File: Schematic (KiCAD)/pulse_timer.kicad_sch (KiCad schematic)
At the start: 50 parts, among them J66 Counter 4 Preload, J70 Counter 4 Preload

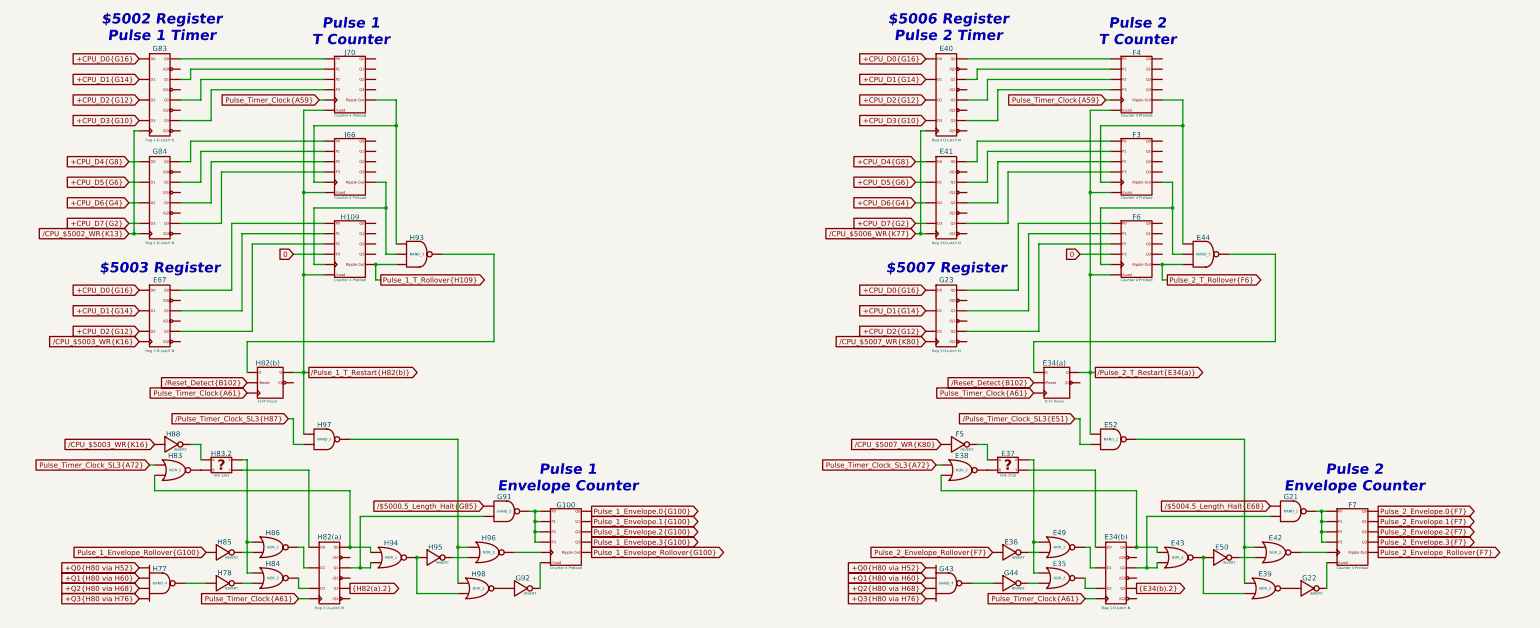
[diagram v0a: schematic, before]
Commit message: - Lots of additional comments and signal name improvements.  - "Don't know what this is yet but it is important" section of the pulse channels:    - I worked out the logic and it is a 4-bit binary up-counter with preload, made from gates and D-latches instead of T-flip-flops.    - It is extremely similar to the envelope counter, but takes twice the die space and much more traces.    - None of its outputs go anywhere else, so I believe that it has no actual function.    - It seems to be a previous attempt at making the envelope counter and it got disconnected and left in.    - Each pulse channel has its own copy and I moved both of them to the "Artifacts" sheet.    - The wasted space amounts to about half of one of the large columns on the left side of the die.  - A couple of "OAI2" cells that noted "unclear order": I determined the correct order of the inputs based on several others which were known.  - Deduced the purpose of the 2 separate methods of scanline detection:    - The one looking for 3 consecutive reads finds the start of a scanline.    - The one counting PPU /RD to find PPU cycle 336, finds the end of the scanline.    - I moved these beside each other on the same sheet for clarity.  - A66.5 Changed from Nand to Nor in order to make sense.  - Basic test mode:    - Pin 92: Active low, enables test mode.    - Pin 29: In test mode, it gives external control of "Scanline Start Detection", which is normally done with the familiar 3 matching PPU reads.  When not in test mode, the pin has no function.    - Pin 30: In test mode, it gives external control of "Scanline End Detection", which is normally done by counting PPU /RD to find PPU cycle 336.  It also gives control of "Pulse Length Clock" when in test mode.  When not in test mode, the pin has no function.    - Pin 98/SL3: In test mode, it gives external control of "Pulse Timer Clock".  Whether or not in test mode, this pin low makes the MMC5 pretend $5104 had not yet been written since reset, probably as a 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
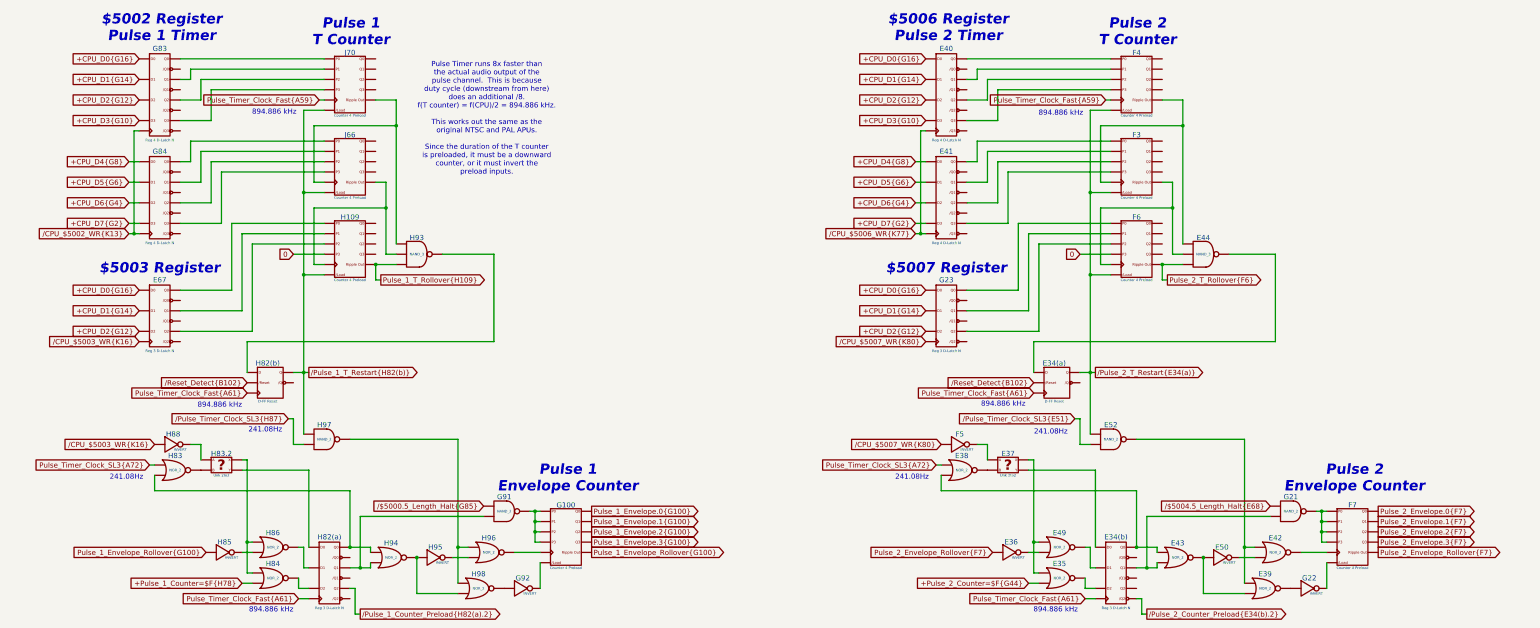
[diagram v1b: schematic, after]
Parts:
- removed G43, H77: NAND_4, symbol MMC5:NAND_4
- removed G44, H78: INVERT, symbol MMC5:INVERT
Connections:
- net {E34(b).2} is gone; now on net /Pulse_2_Counter_Preload{E34(b).2}: E34(b). (/Q2)
- net {H82(a).2} is gone; now on net /Pulse_1_Counter_Preload{H82(a).2}: H82(a). (/Q2)
- net at H86. (X): now also H83.2. (Y), H84. (X); no longer H85. (X)
- net at H83.2. (Y): now also H88. (X); no longer H83. (X)
- net /Pulse_2_Counter_Preload{E34(b).2}: now reaches E34(b). (/Q2)
- net at E37. (Y): now also E38. (X); no longer E34(b). (/Q2)
- net +Pulse_2_Counter=$F{G44}: now reaches E35. (X)
- net +Pulse_2_Counter=$F{G44}: no longer E34(b). (/Q2)
- net at E49. (X): now also E36. (X); no longer E34(b). (/Q2)
- net /Pulse_1_Counter_Preload{H82(a).2}: now reaches H82(a). (/Q2)
- net /Pulse_1_Counter_Preload{H82(a).2}: no longer H86. (X)
- net +Pulse_1_Counter=$F{H78}: now reaches H84. (X)
- net +Pulse_1_Counter=$F{H78}: no longer H82(a). (/Q2)
- net at H96. (X): now also H97. (X), H98. (X); no longer G100. (Ripple_Out)
- net at G92. (X): now also H98. (X); no longer G100. (Ripple_Out)
- net at E42. (X): now also E50. (X); no longer F7. (Ripple_Out)
- net at E50. (X): now also E39. (X), E43. (X); no longer E42. (X)
- removed net Pulse_Timer_Clock{A59}: F4. (Ripple_Out), J70. (Ripple_Out)
- removed net Pulse_Timer_Clock{A61}: E34(a). (/Q), E34(b). (/Q2), H82(a). (/Q2), H82(b). (/Q)
- new net: F6. (Ripple_Out), G23. (/Q2) (x3)
- new net: H85. (X), H86. (X)
- new net: H82(a). (/Q2), H83. (X), H94. (X)
- new net: H83. (X), H83.2. (Y)
- new net: E40. (/Q3), F4. (Ripple_Out) (x4)
- new net: E34(b). (/Q2), E37. (Y)
- new net: E34(b). (/Q2), E43. (X), G21. (X)
- new net: E34(b). (/Q2), E35. (X)
- new net: E34(b). (/Q2), E49. (X)
- new net: E34(b). (/Q2), E38. (X), E43. (X)
- new net: E35. (X), E37. (Y), E49. (X)
- new net: E37. (Y), F5. (X)
- new net: H109. (Ripple_Out), H93. (X), J66. (Ripple_Out)
- new net: H93. (X), J66. (Ripple_Out), J70. (Ripple_Out)
- new net: H82(b). (/Q), H93. (X)
- new net: E67. (/Q2), H109. (Ripple_Out) (x3)
- new net: F7. (Ripple_Out), G21. (X)
- new net: H82(a). (/Q2), H86. (X)
- new net: G91. (X), H82(a). (/Q2), H94. (X)
- new net: G100. (Ripple_Out), G91. (X)
- new net: E41. (/Q3), F3. (Ripple_Out) (x4)
- new net: E44. (X), F3. (Ripple_Out), F6. (Ripple_Out)
- new net: H82(a). (/Q2), H83.2. (Y)
- new net: H82(a). (/Q2), H84. (X)
- new net: H94. (X), H95. (X), H98. (X)
- new net: G100. (Ripple_Out), H96. (X)
- new net: G100. (Ripple_Out), G92. (X)
- new net: G84. (/Q3), J66. (Ripple_Out) (x4)
- new net: E39. (X), E42. (X), E52. (X)
- new net: E42. (X), F7. (Ripple_Out)
- new net: E44. (X), F3. (Ripple_Out), F4. (Ripple_Out)
- new net: G83. (/Q3), J70. (Ripple_Out) (x4)
- new net: E34(a). (/Q), E44. (X)
- new net Pulse_Timer_Clock_Fast{A59}: F4. (Ripple_Out), J70. (Ripple_Out)
- new net Pulse_Timer_Clock_Fast{A61}: E34(a). (/Q), E34(b). (/Q2), H82(a). (/Q2), H82(b). (/Q)
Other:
- note added: "241.08Hz"
- note added: "894.886 kHz"
- note added: "Pulse Timer runs 8x faster than the actual audio output of the pulse channel. This is because duty cycle (downstream from here) does an additional /8. f(T counter) = f(CPU)/2 = 894.886 kHz. This works out the same as the original NTSC and PAL APUs. Since the duration of the T counter is preloaded, it must be a downward counter, or it must invert the preload inputs."

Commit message: - Updated all of the various And-OR-Invert gates to have consistent names.  - Added the schematic for CL3 / SL3 GPIO pins.  There are no surprises revealed by this.  - Finished up the CPU address decoding tracing.  - Added one of the 'artifact' counters from the pulse channels
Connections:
- net at H86. (X): now also H83.2. (Y), H84. (X); no longer H85. (X)
- net at H83.2. (Y): now also H88. (X); no longer H83. (X)
- net at E37. (Y): now also E38. (X); no longer E34(b). (/Q2)
- net at E49. (X): now also E36. (X); no longer E34(b). (/Q2)
- net at H96. (X): now also H97. (X), H98. (X); no longer G100. (Ripple_Out)
- net at G92. (X): now also H98. (X); no longer G100. (Ripple_Out)
- net at E42. (X): now also E50. (X); no longer F7. (Ripple_Out)
- net at E50. (X): now also E39. (X), E43. (X); no longer E42. (X)
- new net: F6. (Ripple_Out), G23. (/Q2) (x3)
- new net: H85. (X), H86. (X)
- new net: H82(a). (/Q2), H83. (X), H94. (X)
- new net: H83. (X), H83.2. (Y)
- new net: E40. (/Q3), F4. (Ripple_Out) (x4)
- new net: E34(b). (/Q2), E37. (Y)
- new net: E34(b). (/Q2), E43. (X), G21. (X)
- new net: E34(b). (/Q2), E35. (X)
- new net: E34(b). (/Q2), E49. (X)
- new net: E34(b). (/Q2), E38. (X), E43. (X)
- new net: E35. (X), E37. (Y), E49. (X)
- new net: E37. (Y), F5. (X)
- new net: H109. (Ripple_Out), H93. (X), J66. (Ripple_Out)
- new net: H93. (X), J66. (Ripple_Out), J70. (Ripple_Out)
- new net: H82(b). (/Q), H93. (X)
- new net: E67. (/Q2), H109. (Ripple_Out) (x3)
- new net: F7. (Ripple_Out), G21. (X)
- new net: H82(a). (/Q2), H86. (X)
- new net: G91. (X), H82(a). (/Q2), H94. (X)
- new net: G100. (Ripple_Out), G91. (X)
- new net: E41. (/Q3), F3. (Ripple_Out) (x4)
- new net: E44. (X), F3. (Ripple_Out), F6. (Ripple_Out)
- new net: H82(a). (/Q2), H83.2. (Y)
- new net: H82(a). (/Q2), H84. (X)
- new net: H94. (X), H95. (X), H98. (X)
- new net: G100. (Ripple_Out), H96. (X)
- new net: G100. (Ripple_Out), G92. (X)
- new net: G84. (/Q3), J66. (Ripple_Out) (x4)
- new net: E39. (X), E42. (X), E52. (X)
- new net: E42. (X), F7. (Ripple_Out)
- new net: E44. (X), F3. (Ripple_Out), F4. (Ripple_Out)
- new net: G83. (/Q3), J70. (Ripple_Out) (x4)
- new net: E34(a). (/Q), E44. (X)
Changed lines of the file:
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@@
 	)
 	(symbol
+		(lib_name "Reg_3_D-Latch_N_1")
 		(lib_id "MMC5:Reg_3_D-Latch_N")
 		(at 243.84 81.28 0)
@@
 	)
 	(symbol
-		(lib_name "INVERT_2")
 		(lib_id "MMC5:INVERT")
 		(at 66.04 148.59 0)
@@
 	)
 	(symbol
-		(lib_name "NOR_2_2")
 		(lib_id "MMC5:NOR_2")
 		(at 53.34 128.27 0)
@@
 	)
 	(symbol
-		(lib_name "Reg_4_D-Latch_N_1")
+		(lib_name "Reg_4_D-Latch_N_2")
 		(lib_id "MMC5:Reg_4_D-Latch_N")
 		(at 243.84 24.13 0)
@@
 	)
 	(symbol
-		(lib_name "Reg_3_D-Latch_N_2")
 		(lib_id "MMC5:Reg_3_D-Latch_N")
 		(at 285.75 144.78 0)
@@
 	)
 	(symbol
-		(lib_name "UNKNOWN_2to2_1")
 		(lib_id "MMC5:UNKNOWN_2to2")
 		(at 259.08 129.54 0)
@@
 	)
 	(symbol
-		(lib_name "Counter_4_Preload_7")
 		(lib_id "MMC5:Counter_4_Preload")
 		(at 96.52 71.12 0)
@@
 	)
 	(symbol
-		(lib_name "NAND_2_2")
+		(lib_name "NAND_2_1")
 		(lib_id "MMC5:NAND_2")
 		(at 328.93 138.43 0)
@@
 	)
 	(symbol
-		(lib_name "Reg_3_D-Latch_N_1")
+		(lib_name "Reg_3_D-Latch_N_2")
 		(lib_id "MMC5:Reg_3_D-Latch_N")
 		(at 49.53 81.28 0)
@@
 	)
 	(symbol
+		(lib_name "NOR_2_1")
 		(lib_id "MMC5:NOR_2")
 		(at 77.47 147.32 0)
@@
 	)
 	(symbol
-		(lib_name "INVERT_7")
+		(lib_name "INVERT_3")
 		(lib_id "MMC5:INVERT")
 		(at 260.35 148.59 0)
@@
 	)
 	(symbol
-		(lib_name "Reg_4_D-Latch_N_2")
+		(lib_name "Reg_4_D-Latch_N_1")
 		(lib_id "MMC5:Reg_4_D-Latch_N")
 		(at 243.84 49.53 0)
@@
 	)
 	(symbol
-		(lib_name "Counter_4_Preload_2")
+		(lib_name "Counter_4_Preload_1")
 		(lib_id "MMC5:Counter_4_Preload")
 		(at 290.83 71.12 0)
@@
 	)
 	(symbol
-		(lib_name "INVERT_4")
+		(lib_name "INVERT_1")
 		(lib_id "MMC5:INVERT")
 		(at 118.11 149.86 0)
@@
 	)
 	(symbol
-		(lib_name "Counter_4_Preload_3")
+		(lib_name "Counter_4_Preload_2")
 		(lib_id "MMC5:Counter_4_Preload")
 		(at 149.86 142.24 0)
@@
 	)
 	(symbol
-		(lib_name "Reg_4_D-Latch_N_5")
 		(lib_id "MMC5:Reg_4_D-Latch_N")
 		(at 49.53 49.53 0)
@@
 	)
 	(symbol
-		(lib_name "NOR_2_6")
+		(lib_name "NOR_2_7")
 		(lib_id "MMC5:NOR_2")
 		(at 325.12 148.59 0)
@@
 	)
 	(symbol
-		(lib_name "NOR_2_9")
+		(lib_name "NOR_2_2")
 		(lib_id "MMC5:NOR_2")
 		(at 271.78 154.94 0)
@@
 	)
 	(symbol
+		(lib_name "Counter_4_Preload_3")
 		(lib_id "MMC5:Counter_4_Preload")
 		(at 290.83 30.48 0)
@@
 	)
 	(symbol
-		(lib_name "Counter_4_Preload_6")
+		(lib_name "Counter_4_Preload_4")
 		(lib_id "MMC5:Counter_4_Preload")
 		(at 96.52 30.48 0)
@@
 	)
 	(symbol
+		(lib_name "UNKNOWN_2to2_1")
 		(lib_id "MMC5:UNKNOWN_2to2")
 		(at 64.77 129.54 0)
@@
 	)
 	(symbol
-		(lib_name "INVERT_9")
+		(lib_name "INVERT_2")
 		(lib_id "MMC5:INVERT")
 		(at 247.65 121.92 0)
@@
 	)
 	(symbol
-		(lib_name "NOR_2_7")
+		(lib_name "NOR_2_6")
 		(lib_id "MMC5:NOR_2")
 		(at 322.58 157.48 0)
@@
 	)
 	(symbol
-		(lib_name "NAND_2_3")
+		(lib_name "NAND_2_2")
 		(lib_id "MMC5:NAND_2")
 		(at 284.48 120.65 0)
@@
 	)
 	(symbol
-		(lib_name "NOR_2_1")
+		(lib_name "NOR_2_8")
 		(lib_id "MMC5:NOR_2")
 		(at 77.47 154.94 0)
@@
 	)
 	(symbol
-		(lib_name "Counter_4_Preload_1")
+		(lib_name "Counter_4_Preload_5")
 		(lib_id "MMC5:Counter_4_Preload")
 		(at 290.83 50.8 0)
@@
 	)
 	(symbol
-		(lib_name "Counter_4_Preload_4")
+		(lib_name "Counter_4_Preload_6")
 		(lib_id "MMC5:Counter_4_Preload")
 		(at 344.17 142.24 0)
@@
 	)
 	(symbol
-		(lib_name "NOR_2_10")
+		(lib_name "NOR_2_3")
 		(lib_id "MMC5:NOR_2")
 		(at 271.78 147.32 0)
@@
 	)
 	(symbol
-		(lib_name "NOR_2_8")
+		(lib_name "NOR_2_4")
 		(lib_id "MMC5:NOR_2")
 		(at 300.99 149.86 0)
@@
 	)
 	(symbol
-		(lib_name "INVERT_6")
+		(lib_name "INVERT_5")
 		(lib_id "MMC5:INVERT")
 		(at 312.42 149.86 0)
@@
 	)
 	(symbol
-		(lib_name "NOR_2_4")
+		(lib_name "NOR_2_9")
 		(lib_id "MMC5:NOR_2")
 		(at 106.68 149.86 0)
@@
 	)
 	(symbol
-		(lib_name "NOR_2_3")
+		(lib_name "NOR_2_10")
 		(lib_id "MMC5:NOR_2")
 		(at 130.81 148.59 0)
@@
 	)
 	(symbol
-		(lib_name "NAND_2_1")
+		(lib_name "NAND_2_3")
 		(lib_id "MMC5:NAND_2")
 		(at 90.17 120.65 0)
@@
 	)
 	(symbol
-		(lib_name "INVERT_10")
+		(lib_name "INVERT_4")
 		(lib_id "MMC5:INVERT")
 		(at 53.34 121.92 0)
@@
 	)
 	(symbol
-		(lib_name "INVERT_5")
+		(lib_name "INVERT_6")
 		(lib_id "MMC5:INVERT")
 		(at 334.01 157.48 0)
@@
 	)
 	(symbol
-		(lib_name "INVERT_3")
+		(lib_name "INVERT_7")
 		(lib_id "MMC5:INVERT")
 		(at 139.7 157.48 0)
@@
 	)
 	(symbol
-		(lib_name "Reg_4_D-Latch_N_4")
+		(lib_name "Reg_4_D-Latch_N_3")
 		(lib_id "MMC5:Reg_4_D-Latch_N")
 		(at 49.53 24.13 0)
@@
 	)
 	(symbol
-		(lib_name "Counter_4_Preload_8")
+		(lib_name "Counter_4_Preload_7")
 		(lib_id "MMC5:Counter_4_Preload")
 		(at 96.52 50.8 0)
